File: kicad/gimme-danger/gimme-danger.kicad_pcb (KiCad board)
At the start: 4 copper layers, 60.1 x 30 mm, 49 parts, among them J1 Screw_Terminal_01x04, Q1 AO3400A, Q2 AO3400A, U1 ESP32-S3-WROOM-1, U2 TPD6S300RUKR, U3 U261-241N-4BS2SS, U4 NX20P5090UKAZ, U5 SKRKAEE020, U7 SKRKAEE020, U8 TPS54302

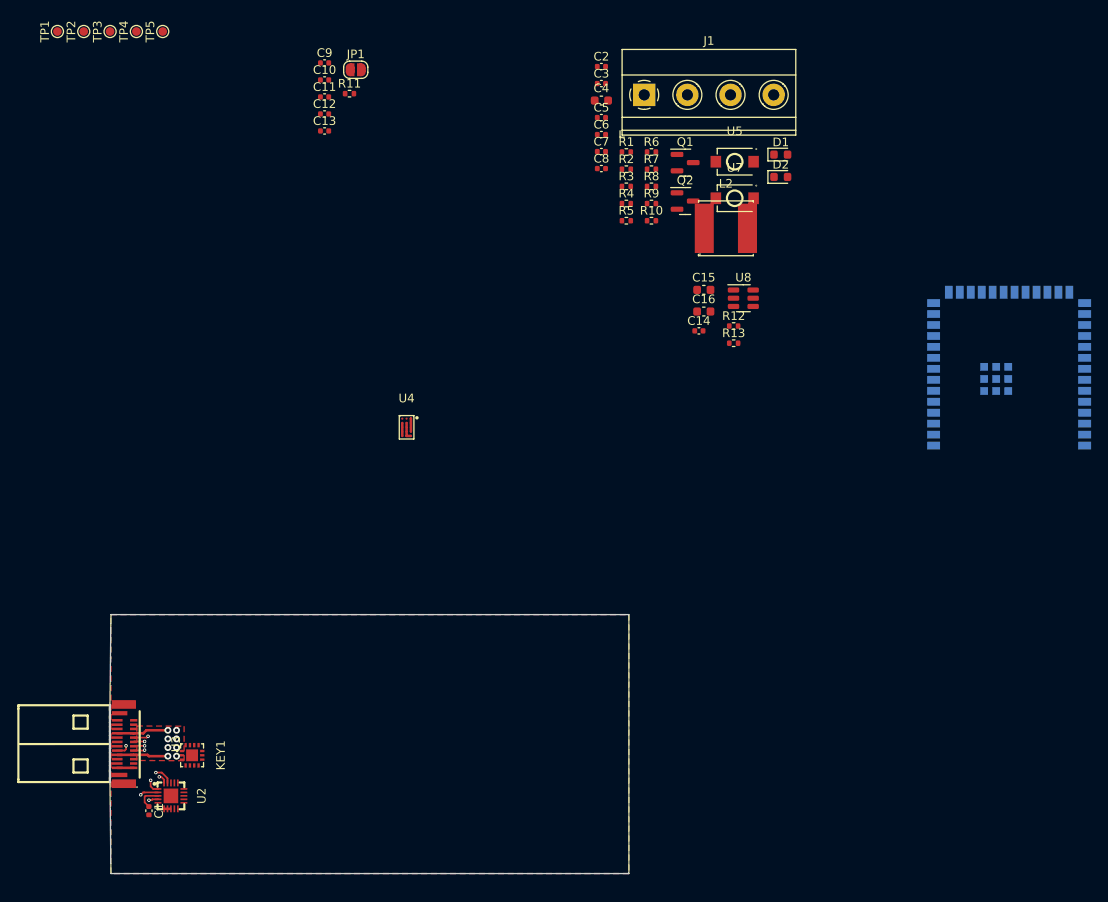
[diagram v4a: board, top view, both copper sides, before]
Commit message: Initial partial routing
But I'm not convinced I can route the tiny load switch well. I will
change it back to the same setup as used by luz.
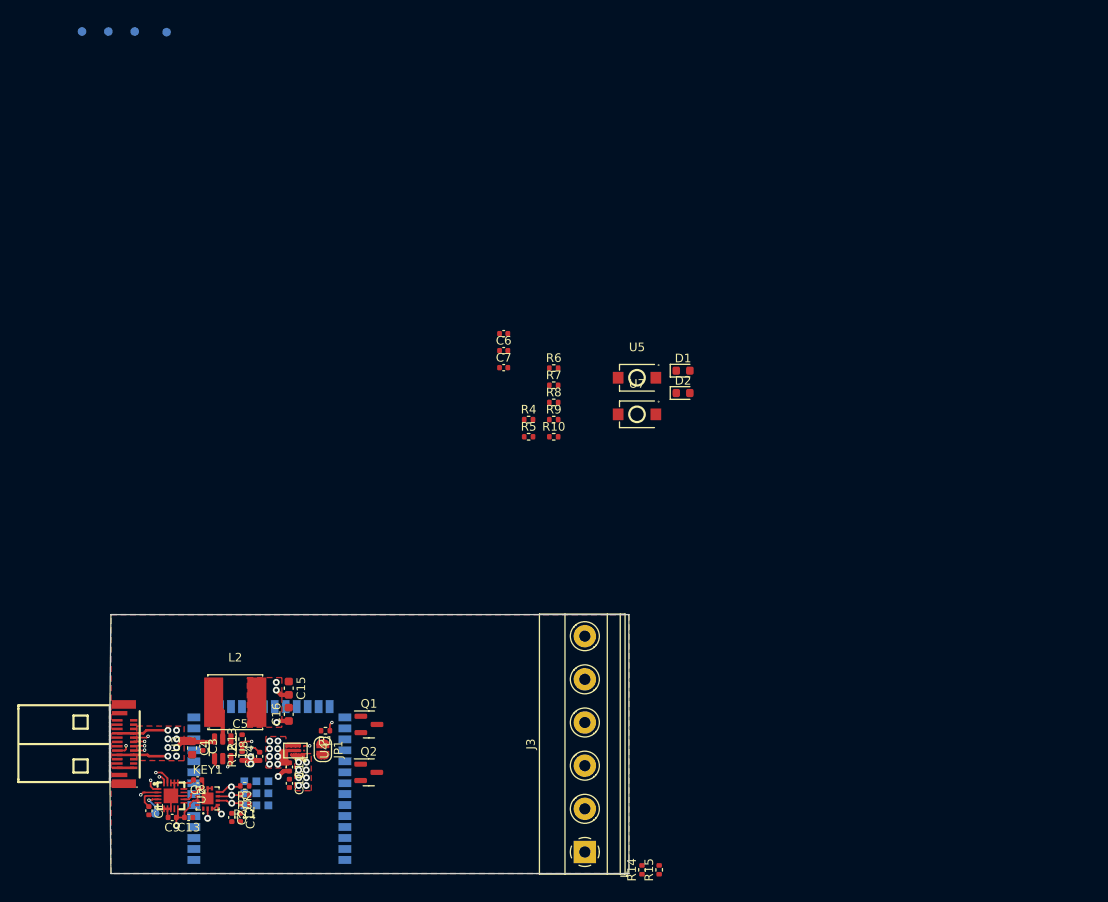
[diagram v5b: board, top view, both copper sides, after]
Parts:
- removed J1: Screw_Terminal_01x04, TerminalBlock_Phoenix:TerminalBlock_Phoenix_MKDS-1,5-4_1x04_P5.00mm_Horizontal
- added J3: Screw_Terminal_01x06, TerminalBlock_Phoenix:TerminalBlock_Phoenix_MKDS-1,5-6_1x06_P5.00mm_Horizontal, F.Cu at (115.9, 124.5)
- added R14: 10k, Resistor_SMD:R_0402_1005Metric, F.Cu at (122.5, 126.6)
- added R15: 10k, Resistor_SMD:R_0402_1005Metric, F.Cu at (124.5, 126.6)
- R13: value 100k -> 22k
- TP1, TP2, TP3, TP4, TP5: moved to B.Cu
- moved U1 98.2 mm to (79.3, 117.2)
- moved C2 97.0 mm to (75.0, 120.5), turned to -90 degrees
- moved TP5 90.6 mm to (66.1, 120.0), turned to 0 degrees
- moved C3 89.6 mm to (71.7, 112.2), turned to -90 degrees
- moved C9 89.2 mm to (68.1, 120.5), turned to 180 degrees
- moved C4 88.7 mm to (70.4, 112.5), turned to -90 degrees
- moved C8 84.9 mm to (71.0, 116.2), turned to 180 degrees
- moved R2 84.0 mm to (76.5, 116.8), turned to 180 degrees
- moved R3 83.2 mm to (76.5, 117.9), turned to 180 degrees
- moved R11 83.2 mm to (76.5, 119.0), turned to 180 degrees
- moved C12 82.1 mm to (76.0, 120.5), turned to -90 degrees
- moved C10 81.6 mm to (81.7, 116.5), turned to -90 degrees
- moved C13 81.1 mm to (70.0, 120.5), turned to 180 degrees
- moved U8 79.8 mm to (74.0, 112.5), turned to -90 degrees
- moved L2 79.0 mm to (75.4, 107.2)
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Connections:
- TP5 pad 1: CC1 -> C_CC1
- U8 pad 3: unconnected-(U8-VIN-Pad3) -> VBUS
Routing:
- net VBUS: track 14.6 -> 36.8 mm, vias 8 -> 17
- net +3V3: track 0.00 -> 16.6 mm, vias 0 -> 8
- net GND: track 4.16 -> 17.8 mm, vias 0 -> 1
- net Net-(U8-FB): track 0.00 -> 9.63 mm, vias 0 -> 2
- net Net-(U8-BOOT): track 0.00 -> 5.94 mm, vias 0 -> 2
- net Net-(U8-SW): track 0.00 -> 4.70 mm
- net CC1: track 0.00 -> 4.17 mm
- net VINT: track 1.50 -> 5.59 mm, vias 0 -> 8
- net SDA: track 0.00 -> 3.11 mm, vias 0 -> 1
- net INT: track 0.00 -> 2.78 mm, vias 0 -> 1
- net SCL: track 0.00 -> 2.67 mm, vias 0 -> 1
- net C_CC1: track 8.28 -> 10.1 mm
- net LOAD_EN#: track 0.00 -> 0.67 mm, vias 0 -> 1
- added copper zone on F.Cu, net +3V3
- added copper zone on F.Cu, net VINT

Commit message: Initial partial routing
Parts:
- removed C11: 1u, Capacitor_SMD:C_0402_1005Metric
- removed JP1: ~, Jumper:SolderJumper-2_P1.3mm_Open_RoundedPad1.0x1.5mm
- added D3: 1N5819WS, Diode_SMD:D_SOD-323, F.Cu at (99.5, 107.0)
- added D4: 1N5819WS, Diode_SMD:D_SOD-323, F.Cu at (99.4, 115.9)
- added R16: 1k, Resistor_SMD:R_0402_1005Metric, F.Cu at (70.5, 107.5)
- added U6: DDTC143EUA, footprint:SOT-323-3_L2.0-W1.3-P1.30-LS2.1-BR, F.Cu at (72.0, 105.8)
- U4: value NX20P5090UKAZ -> AO4407A; footprint footprint:WLCSP-15_L2.6-W1.6-R3-C5-P0.50-TL_NXP -> footprint:SOIC-8_L4.9-W3.9-P1.27-LS6.0-BL
- U5, U7: moved to B.Cu
- moved C6 66.2 mm to (70.1, 121.7), turned to 180 degrees
- moved D1 65.5 mm to (81.4, 115.4), turned to 90 degrees
- moved C7 65.4 mm to (70.1, 122.7), turned to 180 degrees
- moved D2 64.8 mm to (79.8, 115.4), turned to 90 degrees
- moved U5 59.9 mm to (93.7, 122.4), turned to 180 degrees
- moved R6 54.4 mm to (81.1, 113.0), turned to -90 degrees
- moved R5 46.8 mm to (80.1, 113.0), turned to -90 degrees
- moved U7 42.0 mm to (93.1, 104.4)
- moved U4 16.5 mm to (67.4, 105.9), turned to 0 degrees
- moved C10 16.1 mm to (72.9, 103.1)
- moved R1 15.3 mm to (70.5, 109.4), turned to 90 degrees
- moved Q2 9.43 mm to (99.6, 118.9)
- moved Q1 8.90 mm to (99.8, 109.7)
- moved C15 2.00 mm to (83.6, 105.5)
- moved C16 2.00 mm to (83.6, 108.5), turned to -90 degrees
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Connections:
- net Net-(J3-Pin_4) renamed OUT1
- net Net-(J3-Pin_6) renamed OUT2
- C10 pad 1: VINT -> VOUT
- J3 pad 1: VINT -> VOUT
- J3 pad 3: VINT -> VOUT
- J3 pad 5: VINT -> VOUT
- R1 pad 1: +3V3 -> VBUS
- R1 pad 2: Net-(JP1-A) -> Net-(U4-G)
- R8 pad 1: VINT -> VOUT
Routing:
- net Net-(U1-EN): track 0.00 -> 24.7 mm, vias 0 -> 2
- net +3V3: track 16.6 -> 31.4 mm, vias 8 -> 12
- net LOAD_EN#: track 0.67 -> 10.2 mm
- net VBUS: track 36.8 -> 28.7 mm, vias 17 -> 9
- net VINT: track 5.59 -> 0.00 mm, vias 8 -> 0
- net LED_RED: track 0.00 -> 5.05 mm, vias 0 -> 1
- net GND: track 17.8 -> 12.8 mm, vias 1 -> 0
- net LED_GREEN: track 0.00 -> 4.87 mm, vias 0 -> 1
- net Net-(U4-G): track 0.00 -> 2.37 mm
- net VOUT: track 0.00 -> 2.30 mm, vias 0 -> 10
- added copper zone on F.Cu, net VOUT
- added copper zone on In1.Cu, net VOUT
- removed copper zone on In1.Cu, net VBUS
- removed copper zone on F.Cu, net VINT

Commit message: Initial routing
Many issues :|
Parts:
- U5, U7: moved to F.Cu
- moved TP3 82.0 mm to (91.4, 104.1), turned to 180 degrees
- moved TP2 79.8 mm to (88.9, 104.1), turned to 180 degrees
- moved TP4 79.2 mm to (94.0, 104.1), turned to 180 degrees
- moved TP1 78.0 mm to (86.4, 104.1), turned to 180 degrees
- moved C5 60.4 mm to (80.0, 118.7)
- moved R7 59.3 mm to (81.8, 121.2)
- moved R8 59.2 mm to (78.8, 121.2)
- moved R4 54.0 mm to (80.0, 119.8)
- moved R10 48.3 mm to (89.2, 118.8)
- moved R9 40.9 mm to (89.3, 108.2), turned to 180 degrees
- moved R14 37.5 mm to (89.3, 109.2), turned to 180 degrees
- moved R15 35.9 mm to (89.2, 119.8), turned to 180 degrees
- moved J3 14.0 mm to (101.9, 124.5)
- moved U7 12.5 mm to (85.0, 113.9), turned to -90 degrees
- moved U5 8.82 mm to (84.9, 121.4), turned to 90 degrees
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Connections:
- J3 pad 2: GND -> OUT2
- J3 pad 6: OUT2 -> GND
- R10 pad 1: Net-(U1-GPIO18/U1RXD/ADC2_CH7/CLK_OUT3) -> Net-(U1-GPIO47/SPICLK_P/SUBSPICLK_P_DIFF)
- R9 pad 1: Net-(U1-GPIO17/U1TXD/ADC2_CH6) -> CH1
- R9 pad 2: CH1 -> Net-(U1-GPIO48/SPICLK_N/SUBSPICLK_N_DIFF)
- U1 pad 10: Net-(U1-GPIO17/U1TXD/ADC2_CH6) -> unconnected-(U1-GPIO17/U1TXD/ADC2_CH6-Pad10)
- U1 pad 11: Net-(U1-GPIO18/U1RXD/ADC2_CH7/CLK_OUT3) -> unconnected-(U1-GPIO18/U1RXD/ADC2_CH7/CLK_OUT3-Pad11)
- U1 pad 24: unconnected-(U1-GPIO47/SPICLK_P/SUBSPICLK_P_DIFF-Pad24) -> Net-(U1-GPIO47/SPICLK_P/SUBSPICLK_P_DIFF)
- U1 pad 25: unconnected-(U1-GPIO48/SPICLK_N/SUBSPICLK_N_DIFF-Pad25) -> Net-(U1-GPIO48/SPICLK_N/SUBSPICLK_N_DIFF)
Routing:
- net TX: track 0.00 -> 21.8 mm, vias 0 -> 2
- net RX: track 0.00 -> 21.5 mm, vias 0 -> 2
- net SCL: track 2.67 -> 23.7 mm, vias 1 -> 2
- net INT: track 2.78 -> 20.1 mm, vias 1 -> 2
- net Net-(U1-GPIO47/SPICLK_P/SUBSPICLK_P_DIFF): track 0.00 -> 13.7 mm, vias 0 -> 1
- net VMON: track 0.00 -> 10.5 mm, vias 0 -> 2
- net SDA: track 3.11 -> 12.1 mm, vias 1 -> 2
- net D+: track 7.33 -> 16.0 mm
- net D-: track 7.47 -> 14.8 mm
- net Net-(U1-GPIO48/SPICLK_N/SUBSPICLK_N_DIFF): track 0.00 -> 5.90 mm, vias 0 -> 1
- net Net-(U1-EN): track 24.7 -> 19.1 mm
- net Net-(U1-GPIO0/BOOT): track 0.00 -> 4.58 mm, vias 0 -> 1
- net +3V3: track 31.4 -> 35.8 mm, vias 12 -> 13
- net CH2: track 0.00 -> 2.65 mm
- net CH1: track 0.00 -> 2.60 mm
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- added copper zone on F.Cu, net OUT1
- added copper zone on F.Cu, net OUT2
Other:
- board size 60.1 x 30 mm -> 46.1 x 30 mm

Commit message: DRC kinda passes
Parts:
- moved C12 0.30 mm to (76.0, 120.8)
- moved C2 0.30 mm to (75.0, 120.8)
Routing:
- net GND: track 12.8 -> 31.7 mm, vias 0 -> 18
- net INT: track 20.1 -> 25.3 mm
- net Net-(U8-FB): track 9.63 -> 12.0 mm, vias 2 -> 3
- net Net-(U8-BOOT): track 5.94 -> 7.58 mm
- net Net-(U6-OUT): track 0.00 -> 1.38 mm
- net C_SBU1: track 10.8 -> 11.7 mm
